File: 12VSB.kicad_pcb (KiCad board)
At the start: 4 copper layers, 16.9 x 17.3 mm, 24 parts, among them U1 FP6296

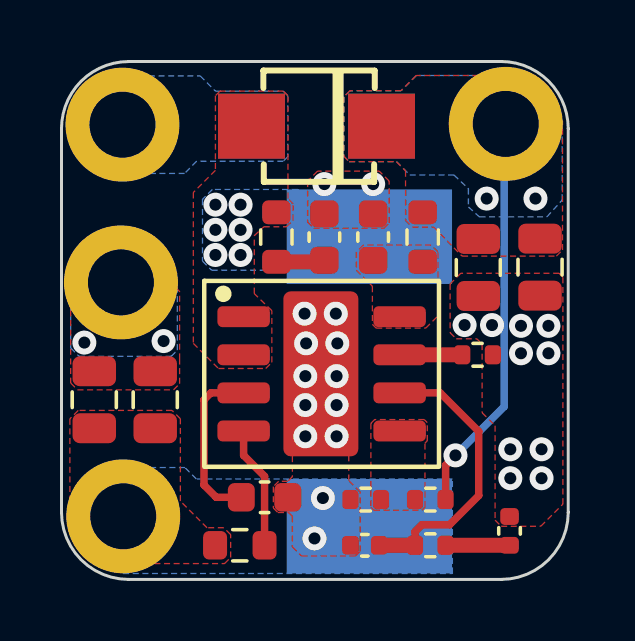
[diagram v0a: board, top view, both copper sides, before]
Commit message: refined schematic and updated pcb layout
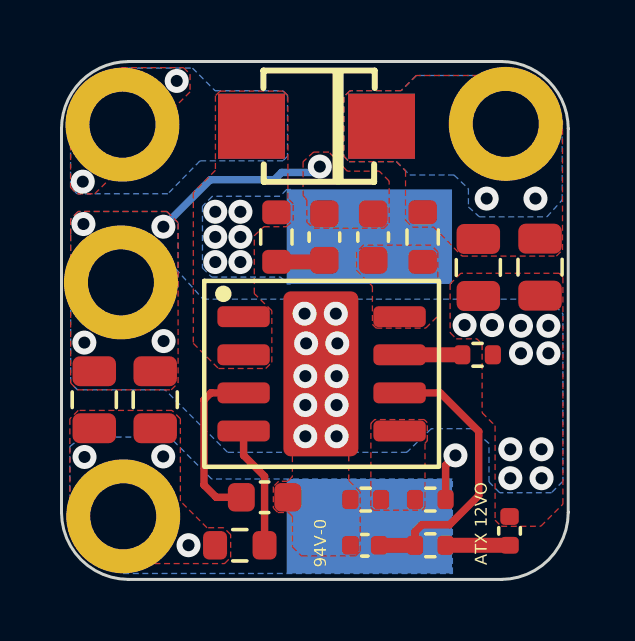
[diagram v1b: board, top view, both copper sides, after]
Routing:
- net GND: track 0.00 -> 6.04 mm, vias 26 -> 25
- net 12VSB: track 13.0 -> 11.2 mm
- net 5VSB: vias 0 -> 3
- net 12V: vias 0 -> 2
- added copper zone on F.Cu, net 12V
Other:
- board text added: "+12VSB"
- board text added: "94V-0"
- board text added: "ATX 12VO"
- board text removed: "12VSB"

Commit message: Refined Silkscreens and added Documentation
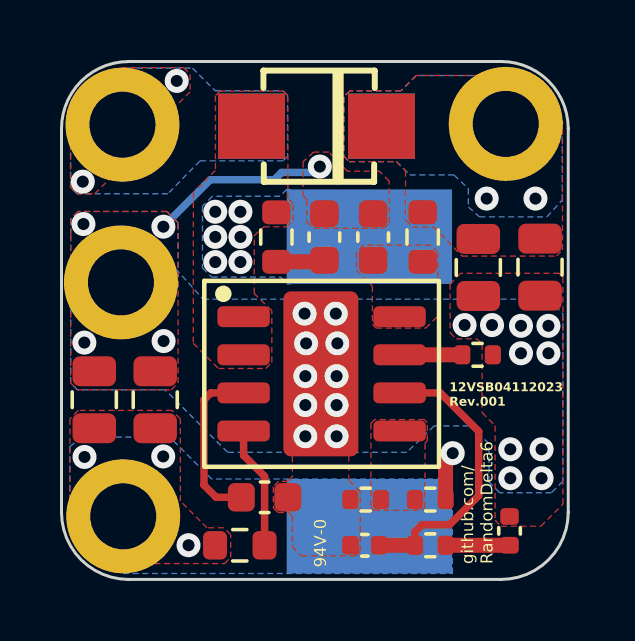
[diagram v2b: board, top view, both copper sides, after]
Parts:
- C1, C2, C5, C6: value C -> C 22uF
- C12: value C -> C 1nF
- C3: value C -> C 1uF
- C9: value C -> C 0.1uF
- D1, D2: value SH548F -> SH54BF
- L1: value L 3R3 -> L 3R3 10A
- R1: value R 30D -> 200K
- R10: value R 102 -> 1K
- R2: value R 223 -> 22K
- R3: value R 01D -> 100K
- R4: value R 303 -> 30K
- R5: value R -> 100
- R8: value R 1R5 -> 1.5
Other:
- board text added: "12VSB04112023 Rev.001"
- board text added: "github.com/ RandomDelta6"
- board text removed: "ATX 12VO"
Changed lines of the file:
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@@
         (effects (font (size 1 1) (thickness 0.15)))
     )
-    (fp_text value "R 30D" (at 0 1.17) (layer "F.Fab")
+    (fp_text value "200K" (at 0 1.17) (layer "F.Fab")
         (effects (font (size 1 1) (thickness 0.15)))
     )
@@
         (effects (font (size 1 1) (thickness 0.15)))
     )
-    (fp_text value "R 102" (at 0 1.43) (layer "F.Fab")
+    (fp_text value "1K" (at 0 1.43) (layer "F.Fab")
         (effects (font (size 1 1) (thickness 0.15)))
     )
@@
         (effects (font (size 1 1) (thickness 0.15)))
     )
-    (fp_text value "R 223" (at 0 1.17) (layer "F.Fab")
+    (fp_text value "22K" (at 0 1.17) (layer "F.Fab")
         (effects (font (size 1 1) (thickness 0.15)))
     )
@@
         (effects (font (size 1 1) (thickness 0.15)))
     )
-    (fp_text value "R" (at -0.919 8.4838 -180) (layer "F.Fab")
+    (fp_text value "100" (at -0.919 8.4838 -180) (layer "F.Fab")
         (effects (font (size 1 1) (thickness 0.15)))
     )
@@
         (effects (font (size 1 1) (thickness 0.15)))
     )
-    (fp_text value "C" (at 0 1.43) (layer "F.Fab")
+    (fp_text value "C 1uF" (at 0 1.43) (layer "F.Fab")
         (effects (font (size 1 1) (thickness 0.15)))
     )
@@
         (effects (font (size 1.27 1.27) (thickness 0.254)))
     )
-    (fp_text value " SH548F" (at 0 0 180) (layer "F.SilkS") hide
+    (fp_text value " SH54BF" (at 0 0 180) (layer "F.SilkS") hide
         (effects (font (size 1.27 1.27) (thickness 0.254)))
     )
@@
         (effects (font (size 1 1) (thickness 0.15)))
     )
-    (fp_text value "R 1R5" (at -0.508 1.43 90) (layer "F.Fab")
+    (fp_text value "1.5" (at -0.508 1.43 90) (layer "F.Fab")
         (effects (font (size 1 1) (thickness 0.15)))
     )
@@
         (effects (font (size 1 1) (thickness 0.15)))
     )
-    (fp_text value "R 01D" (at 1.2446 0) (layer "F.Fab")
+    (fp_text value "100K" (at 1.2446 0) (layer "F.Fab")
         (effects (font (size 1 1) (thickness 0.15)))
     )
@@
         (effects (font (size 1 1) (thickness 0.15)))
     )
-    (fp_text value "C" (at 0 1.43 90) (layer "F.Fab")
+    (fp_text value " C 0.1uF" (at 0 1.43 90) (layer "F.Fab")
         (effects (font (size 1 1) (thickness 0.15)))
     )
@@
         (effects (font (size 1 1) (thickness 0.15)))
     )
-    (fp_text value "C" (at 0 1.68 90) (layer "F.Fab")
+    (fp_text value "C 22uF" (at 0 1.68 90) (layer "F.Fab")
         (effects (font (size 1 1) (thickness 0.15)))
     )
@@
     (pad "9" smd roundrect (at 0 0) (size 2.5 5.5) (layers "F.Cu" "F.Paste" "F.Mask") (roundrect_rratio 0.1)
       (net 2 "GND") (pinfunction "GND") (pintype "passive") (thermal_bridge_angle 45))
+    (model "${KIPRJMOD}/12VSB Library.pretty/fp6296cad.step"
+      (offset (xyz 0 0 0))
+      (scale (xyz 1 1 1))
+      (rotate (xyz 0 0 0))
+    )
   )
   (footprint "Capacitor_SMD:C_0402_1005Metric" (layer "F.Cu")
@@
         (effects (font (size 1 1) (thickness 0.15)))
     )
-    (fp_text value "C" (at 2.195 0.136 90) (layer "F.Fab")
+    (fp_text value "C 22uF" (at 2.195 0.136 90) (layer "F.Fab")
         (effects (font (size 1 1) (thickness 0.15)))
     )
@@
         (effects (font (size 1 1) (thickness 0.15)))
     )
-    (fp_text value "C" (at 0 1.68 90) (layer "F.Fab")
+    (fp_text value "C 22uF" (at 0 1.68 90) (layer "F.Fab")
         (effects (font (size 1 1) (thickness 0.15)))
     )
@@
         (effects (font (size 1 1) (thickness 0.15)))
     )
-    (fp_text value "C" (at 2.377 -0.229 90) (layer "F.Fab")
+    (fp_text value "C 22uF" (at 2.377 -0.229 90) (layer "F.Fab")
         (effects (font (size 1 1) (thickness 0.15)))
     )
@@
         (effects (font (size 1 1) (thickness 0.15)))
     )
-    (fp_text value "C" (at 0 1.43 90) (layer "F.Fab")
+    (fp_text value "C 1nF" (at 0 1.43 90) (layer "F.Fab")
         (effects (font (size 1 1) (thickness 0.15)))
     )
@@
         (effects (font (size 1 1) (thickness 0.15)))
     )
-    (fp_text value "R 303" (at 0 1.17) (layer "F.Fab")
+    (fp_text value "30K" (at 0 1.17) (layer "F.Fab")
         (effects (font (size 1 1) (thickness 0.15)))
     )
@@
         (effects (font (size 1.27 1.27) (thickness 0.254)) (justify mirror))
     )
-    (fp_text value "SH548F" (at 0 0) (layer "B.SilkS") hide
+    (fp_text value "SH54BF" (at 0 0) (layer "B.SilkS") hide
         (effects (font (size 1.27 1.27) (thickness 0.254)) (justify mirror))
     )
@@
         (effects (font (size 1.643118 1.643118) (thickness 0.15)) (justify mirror))
     )
-    (fp_text value "L 3R3" (at 0.5842 0.1016 180) (layer "B.Fab")
+    (fp_text value "L 3R3 10A" (at 0.5842 0.1016 180) (layer "B.Fab")
         (effects (font (size 1.642866 1.642866) (thickness 0.15)) (justify mirror))
     )
@@
     (effects (font (size 0.6 0.6) (thickness 0.1) bold) (justify left bottom mirror))
   )
+  (gr_text "12VSB04112023\nRev.001" (at 65.65646 63.71082) (layer "F.SilkS")
+    (effects (font (size 0.3 0.3) (thickness 0.06) bold) (justify left bottom))
+  )
   (gr_text "94V-0" (at 61.595 69.0626 90) (layer "F.SilkS")
     (effects (font (size 0.4 0.4) (thickness 0.05)) (justify left bottom))
   )
-  (gr_text "ATX 12VO" (at 66.9544 68.9864 90) (layer "F.SilkS")
+  (gr_text "github.com/\nRandomDelta6\n" (at 67.1449 68.95084 90) (layer "F.SilkS")
     (effects (font (size 0.4 0.4) (thickness 0.05)) (justify left bottom))
   )
@@
   (segment (start 57.8866 66.7258) (end 58.7248 66.7258) (width 0.25) (layer "F.Cu") (net 3))
   (segment (start 65.534 68.326) (end 67.6656 68.326) (width 0.5) (layer "F.Cu") (net 4))
-  (segment (start 65.534 65.657) (end 65.534 66.802) (width 0.25) (layer "F.Cu") (net 5))
-  (segment (start 65.8622 65.3288) (end 65.534 65.657) (width 0.25) (layer "F.Cu") (net 5))
+  (segment (start 65.534 66.802) (end 65.534 65.4919) (width 0.5) (layer "F.Cu") (net 5))
+  (segment (start 65.534 65.4919) (end 65.77076 65.25514) (width 0.5) (layer "F.Cu") (net 5))
   (via (at 66.9036 56.769) (size 0.8) (drill 0.4) (layers "F.Cu" "B.Cu") (free) (net 5))
-  (via (at 65.8622 65.3288) (size 0.8) (drill 0.4) (layers "F.Cu" "B.Cu") (free) (net 5))
+  (via (at 65.77076 65.25514) (size 0.8) (drill 0.4) (layers "F.Cu" "B.Cu") (free) (net 5))
   (via (at 68.5292 56.769) (size 0.8) (drill 0.4) (layers "F.Cu" "B.Cu") (free) (net 5))
   (segment (start 66.9036 56.769) (end 65.1002 58.5724) (width 0.5) (layer "In1.Cu") (net 5))
-  (segment (start 65.1002 58.5724) (end 65.1002 64.5668) (width 0.5) (layer "In1.Cu") (net 5))
-  (segment (start 65.1002 64.5668) (end 65.8622 65.3288) (width 0.5) (layer "In1.Cu") (net 5))
+  (segment (start 65.1002 64.58458) (end 65.77076 65.25514) (width 0.5) (layer "In1.Cu") (net 5))
+  (segment (start 65.1002 58.5724) (end 65.1002 64.58458) (width 0.5) (layer "In1.Cu") (net 5))
   (segment (start 63.1682 58.8762) (end 63.119 58.827) (width 0.25) (layer "F.Cu") (net 6))
   (segment (start 66.638 64.5298) (end 66.638 66.668538) (width 0.25) (layer "F.Cu") (net 7))
@@
         (xy 66.9798 66.2178)
         (xy 66.9798 64.929658)
-        (xy 66.408297 64.4398)
-        (xy 65.055524 64.4398)
+        (xy 66.301616 64.34836)
+        (xy 65.150118 64.34836)
         (xy 64.240972 65.2272)
         (xy 58.2676 65.2272)

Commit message: Updated schematic
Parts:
- C1, C2, C5, C6: value C 22uF -> 22uF
- C10: value C -> 470pF
- C12: value C 1nF -> 1nF
- C3: value C 1uF -> 1uF
- C4: value C -> 2.2nF
- C9: value C 0.1uF -> 0.1uF
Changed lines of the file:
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@@
         (effects (font (size 1 1) (thickness 0.15)))
     )
-    (fp_text value "C" (at 0 1.16) (layer "F.Fab")
+    (fp_text value "470pF" (at 0 1.16) (layer "F.Fab")
         (effects (font (size 1 1) (thickness 0.15)))
     )
@@
         (effects (font (size 1 1) (thickness 0.15)))
     )
-    (fp_text value "C 1uF" (at 0 1.43) (layer "F.Fab")
+    (fp_text value "1uF" (at 0 1.43) (layer "F.Fab")
         (effects (font (size 1 1) (thickness 0.15)))
     )
@@
         (effects (font (size 1 1) (thickness 0.15)))
     )
-    (fp_text value " C 0.1uF" (at 0 1.43 90) (layer "F.Fab")
+    (fp_text value "0.1uF" (at 0 1.43 90) (layer "F.Fab")
         (effects (font (size 1 1) (thickness 0.15)))
     )
@@
         (effects (font (size 1 1) (thickness 0.15)))
     )
-    (fp_text value "C 22uF" (at 0 1.68 90) (layer "F.Fab")
+    (fp_text value "22uF" (at 0 1.68 90) (layer "F.Fab")
         (effects (font (size 1 1) (thickness 0.15)))
     )
@@
         (effects (font (size 1 1) (thickness 0.15)))
     )
-    (fp_text value "C" (at 0 1.16 90) (layer "F.Fab")
+    (fp_text value "2.2nF" (at 0 1.16 90) (layer "F.Fab")
         (effects (font (size 1 1) (thickness 0.15)))
     )
@@
         (effects (font (size 1 1) (thickness 0.15)))
     )
-    (fp_text value "C 22uF" (at 2.195 0.136 90) (layer "F.Fab")
+    (fp_text value "22uF" (at 2.195 0.136 90) (layer "F.Fab")
         (effects (font (size 1 1) (thickness 0.15)))
     )
@@
         (effects (font (size 1 1) (thickness 0.15)))
     )
-    (fp_text value "C 22uF" (at 0 1.68 90) (layer "F.Fab")
+    (fp_text value "22uF" (at 0 1.68 90) (layer "F.Fab")
         (effects (font (size 1 1) (thickness 0.15)))
     )
@@
         (effects (font (size 1 1) (thickness 0.15)))
     )
-    (fp_text value "C 22uF" (at 2.377 -0.229 90) (layer "F.Fab")
+    (fp_text value "22uF" (at 2.377 -0.229 90) (layer "F.Fab")
         (effects (font (size 1 1) (thickness 0.15)))
     )
@@
         (effects (font (size 1 1) (thickness 0.15)))
     )
-    (fp_text value "C 1nF" (at 0 1.43 90) (layer "F.Fab")
-        (effects (font (size 1 1) (thickness 0.15)))
-    )
+    (fp_text value "1nF" (at 0 1.43 90) (layer "F.Fab")
+        (effects (font (size 1 1) (thickness 0.15)))
+    )

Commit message: Updated PCB layout
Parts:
- moved C10 7.14 mm to (67.7, 63.1), turned to 0 degrees
- moved R4 4.90 mm to (66.2, 63.6), turned to -90 degrees
- moved C4 3.77 mm to (67.7, 64.1), turned to 0 degrees
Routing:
- net Net-(U1-COMP): track 9.58 -> 3.26 mm
- net Net-(C4-Pad1): track 2.13 -> 1.03 mm
- net 12VSB: track 11.2 -> 10.3 mm
- net GND: vias 25 -> 24
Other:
- board text added: "12VSB04112023 Rev.002"
- board text added: "github.com/RandomDelta6"
- board text removed: "12VSB04112023 Rev.001"
- board text removed: "github.com/ RandomDelta6"
